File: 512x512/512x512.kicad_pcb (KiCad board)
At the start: 2 copper layers, 99.1 x 49.9 mm, 29 parts, among them J1 CONN_01X39, U1 SST39SF040, U2 AS6C4008-55PCN, U3 74LS670, U4 74LS670, U5 74LS139, U6 74LS74, U7 74LS138

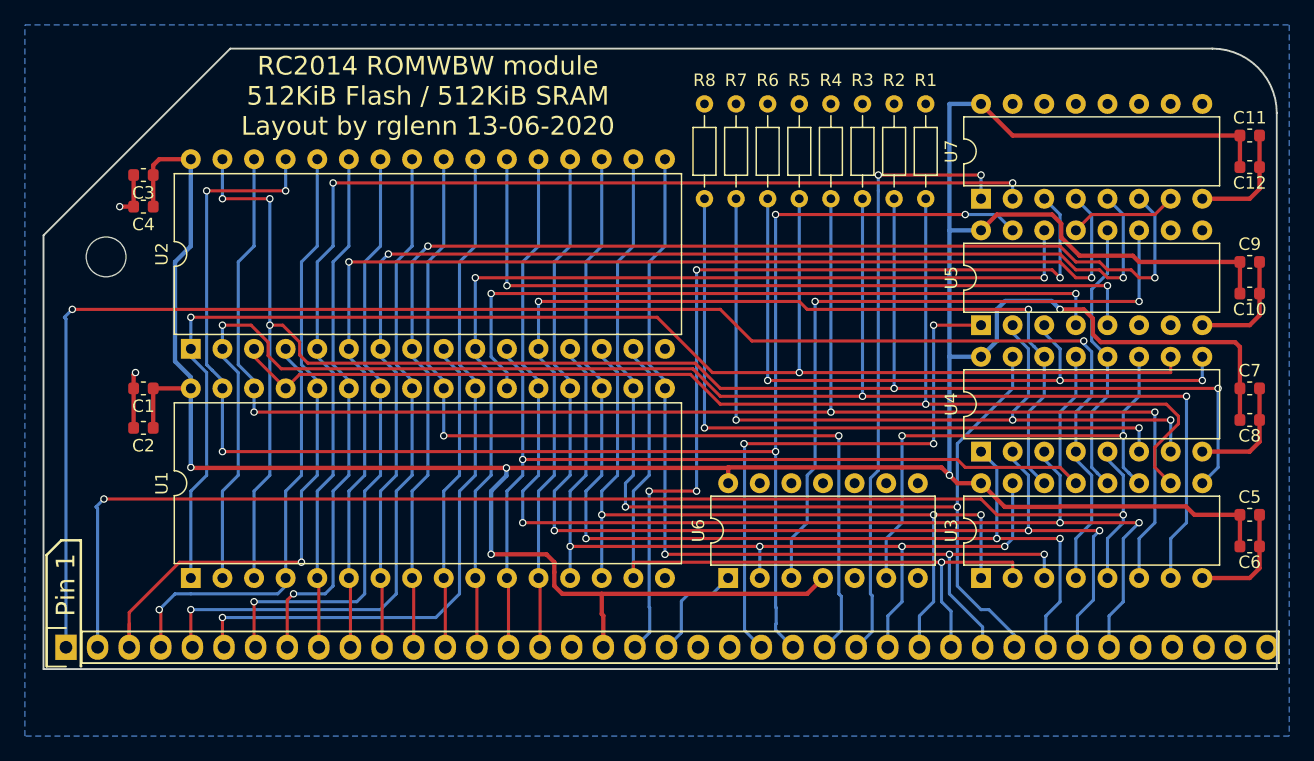
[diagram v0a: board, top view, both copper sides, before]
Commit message: Fixing schematic errors. With these fixes, the thing actually boots.
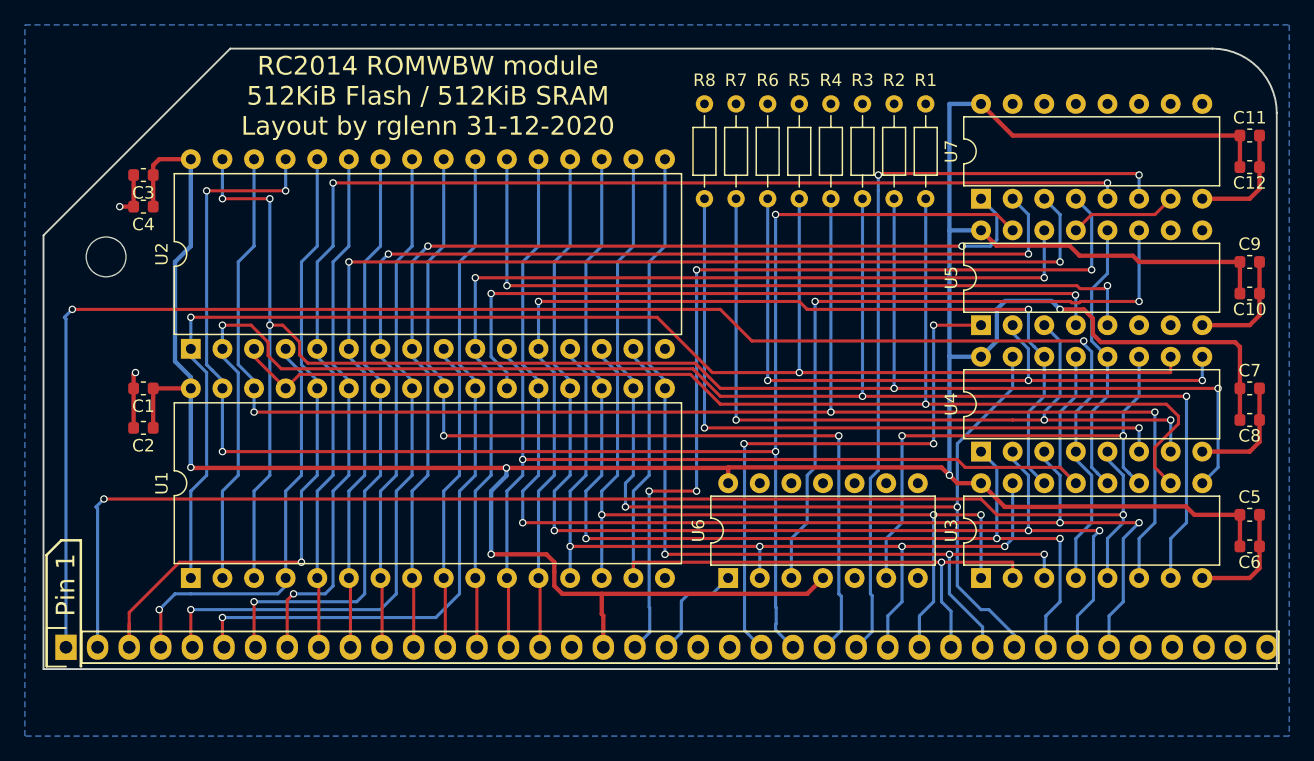
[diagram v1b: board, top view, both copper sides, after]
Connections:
- J1 pad 21: (no net) -> CLK
- J1 pad 22: (no net) -> INT
- J1 pad 35: (no net) -> TX
- J1 pad 36: (no net) -> RX
- J1 pad 37: (no net) -> USR1
- J1 pad 38: (no net) -> USR2
- J1 pad 39: (no net) -> USR3
- U5 pad 10: (no net) -> Net-(U5-Pad10)
- U5 pad 2: MA20 -> MA19
- U5 pad 3: MA19 -> MA20
- U5 pad 6: (no net) -> Net-(U5-Pad6)
- U5 pad 7: (no net) -> Net-(U5-Pad7)
- U5 pad 9: (no net) -> Net-(U5-Pad9)
- U6 pad 5: (no net) -> Net-(U6-Pad5)
- U6 pad 8: (no net) -> Net-(U6-Pad8)
- U6 pad 9: (no net) -> Net-(U6-Pad9)
- U7 pad 1: /IORQ -> A4
- U7 pad 10: (no net) -> Net-(U7-Pad10)
- U7 pad 11: (no net) -> Net-(U7-Pad11)
- U7 pad 12: (no net) -> Net-(U7-Pad12)
- U7 pad 13: (no net) -> Net-(U7-Pad13)
- U7 pad 14: (no net) -> Net-(U7-Pad14)
- U7 pad 15: (no net) -> Net-(U7-Pad15)
- U7 pad 2: A7 -> A5
- U7 pad 3: /M1 -> A6
- U7 pad 4: A6 -> /M1
- U7 pad 5: A5 -> A7
- U7 pad 6: A4 -> /IORQ
- U7 pad 9: (no net) -> Net-(U7-Pad9)
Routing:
- net A4: track 100.2 -> 83.6 mm
- net /IORQ: track 49.0 -> 61.8 mm
- net A5: track 99.7 -> 89.4 mm
- net A7: track 94.8 -> 102.4 mm
- net A6: track 99.2 -> 94.8 mm
- net VCC: track 290.0 -> 288.3 mm
- net /M1: track 71.0 -> 72.6 mm
- net MA20: track 63.9 -> 64.6 mm
- net /WR: vias 6 -> 5
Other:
- board text added: "RC2014 ROMWBW module 512KiB Flash / 512KiB SRAM Layout by rglenn 31-12-2020"
- board text removed: "RC2014 ROMWBW module 512KiB Flash / 512KiB SRAM Layout by rglenn 13-06-2020"

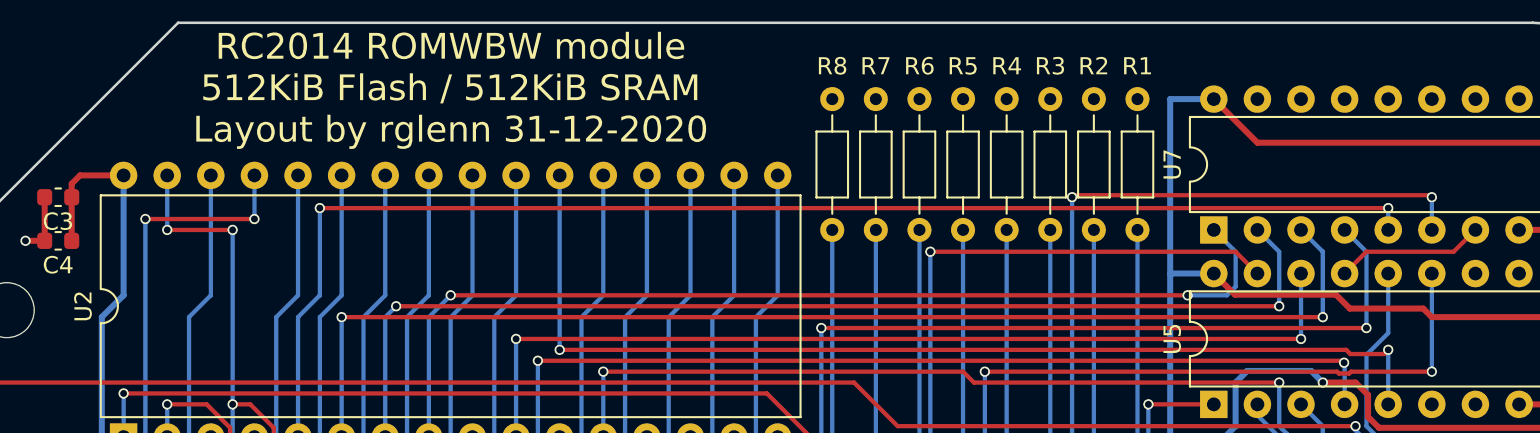
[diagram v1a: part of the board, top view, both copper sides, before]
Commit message: Even with the most recent updates, ~M1 and IOREQ were crossed. Fixed on PCBs here, fixed with wire on the boards I have.
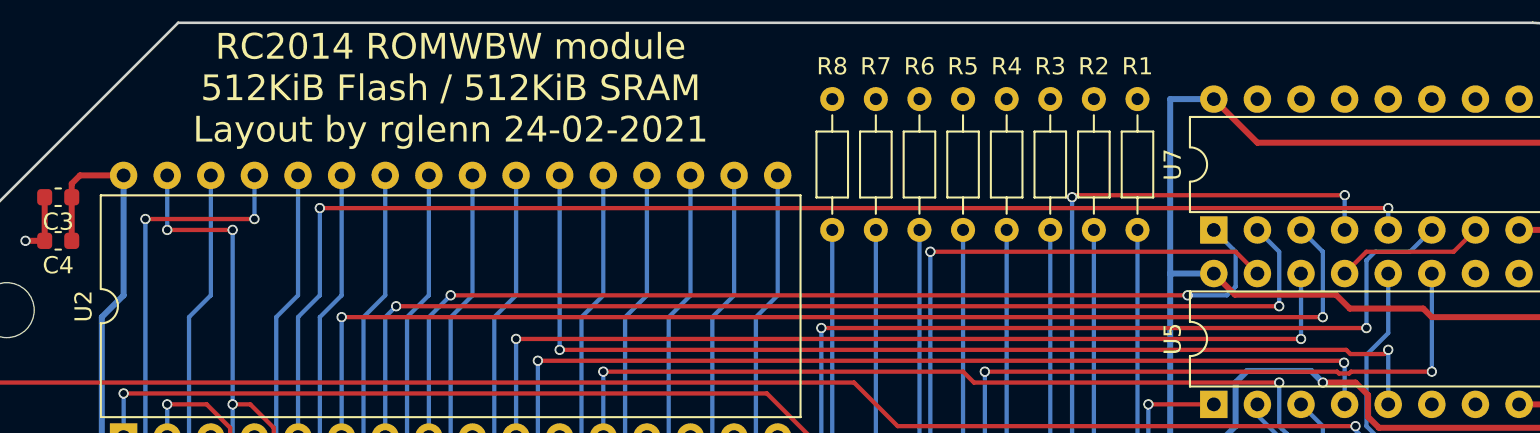
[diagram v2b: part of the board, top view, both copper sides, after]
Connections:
- U7 pad 4: /M1 -> /IORQ
- U7 pad 6: /IORQ -> /M1
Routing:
- net /IORQ: track 61.8 -> 56.8 mm
- net /M1: track 72.6 -> 74.9 mm
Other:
- board text added: "RC2014 ROMWBW module 512KiB Flash / 512KiB SRAM Layout by rglenn 24-02-2021"
- board text removed: "RC2014 ROMWBW module 512KiB Flash / 512KiB SRAM Layout by rglenn 31-12-2020"
